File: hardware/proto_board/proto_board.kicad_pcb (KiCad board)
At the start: 2 copper layers, 120 x 70 mm, 16 parts, among them J01 Conn_02x06_Odd_Even, J010 Screw_Terminal_01x02, J02 Conn_02x06_Odd_Even, J03 Conn_02x06_Odd_Even, J04 Screw_Terminal_01x02, J05 Conn_02x06_Odd_Even, J06 Screw_Terminal_01x02, J07 Screw_Terminal_01x02, J08 Screw_Terminal_01x02, J09 Screw_Terminal_01x02

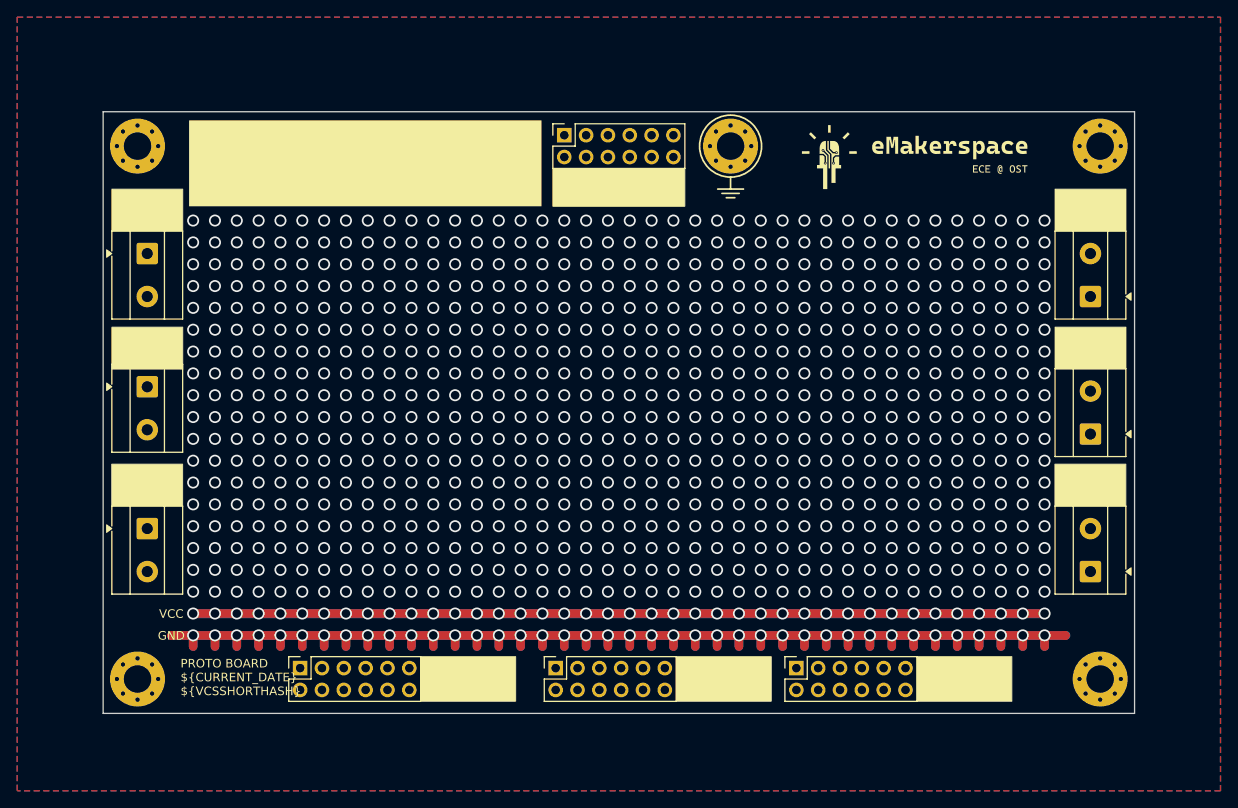
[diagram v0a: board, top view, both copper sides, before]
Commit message: Add solder pads to ribbon cable
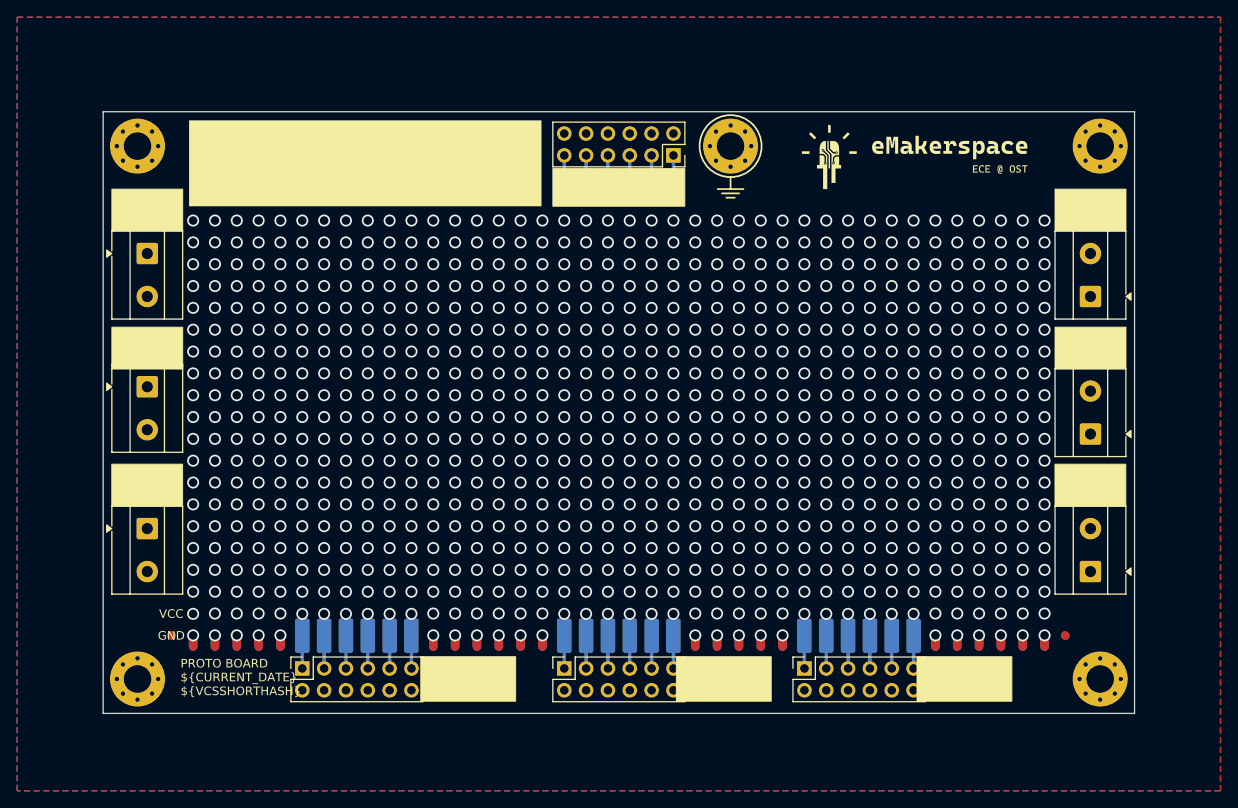
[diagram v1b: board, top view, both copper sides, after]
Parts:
- added J011: Conn_01x06, barbot:6Pin, B.Cu at (136.3, 69.9)
- added J012: Conn_01x06, barbot:6Pin, B.Cu at (93.2, 122.0)
- added J013: Conn_01x06, barbot:6Pin, B.Cu at (123.7, 122.0)
- added J014: Conn_01x06, barbot:6Pin, B.Cu at (151.6, 122.0)
- moved J05 12.9 mm to (136.3, 66.1), turned to -90 degrees
- moved J02 1.00 mm to (123.7, 125.8)
- moved J03 0.94 mm to (151.6, 125.8)
- moved J01 0.25 mm to (93.2, 125.8)
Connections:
- J01 pad 1: unconnected-(J01-Pin_1-Pad1) -> Net-(J01-Pin_1)
- J01 pad 11: unconnected-(J01-Pin_11-Pad11) -> Net-(J01-Pin_11)
- J01 pad 3: unconnected-(J01-Pin_3-Pad3) -> Net-(J01-Pin_3)
- J01 pad 5: unconnected-(J01-Pin_5-Pad5) -> Net-(J01-Pin_5)
- J01 pad 7: unconnected-(J01-Pin_7-Pad7) -> Net-(J01-Pin_7)
- J01 pad 9: unconnected-(J01-Pin_9-Pad9) -> Net-(J01-Pin_9)
- J02 pad 1: unconnected-(J02-Pin_1-Pad1) -> Net-(J013-Pin_1)
- J02 pad 11: unconnected-(J02-Pin_11-Pad11) -> Net-(J013-Pin_6)
- J02 pad 3: unconnected-(J02-Pin_3-Pad3) -> Net-(J013-Pin_2)
- J02 pad 5: unconnected-(J02-Pin_5-Pad5) -> Net-(J013-Pin_3)
- J02 pad 7: unconnected-(J02-Pin_7-Pad7) -> Net-(J013-Pin_4)
- J02 pad 9: unconnected-(J02-Pin_9-Pad9) -> Net-(J013-Pin_5)
- J03 pad 1: unconnected-(J03-Pin_1-Pad1) -> Net-(J014-Pin_1)
- J03 pad 11: unconnected-(J03-Pin_11-Pad11) -> Net-(J014-Pin_6)
- J03 pad 3: unconnected-(J03-Pin_3-Pad3) -> Net-(J014-Pin_2)
- J03 pad 5: unconnected-(J03-Pin_5-Pad5) -> Net-(J014-Pin_3)
- J03 pad 7: unconnected-(J03-Pin_7-Pad7) -> Net-(J014-Pin_4)
- J03 pad 9: unconnected-(J03-Pin_9-Pad9) -> Net-(J014-Pin_5)
- J05 pad 1: unconnected-(J05-Pin_1-Pad1) -> Net-(J011-Pin_1)
- J05 pad 11: unconnected-(J05-Pin_11-Pad11) -> Net-(J011-Pin_6)
- J05 pad 3: unconnected-(J05-Pin_3-Pad3) -> Net-(J011-Pin_2)
- J05 pad 5: unconnected-(J05-Pin_5-Pad5) -> Net-(J011-Pin_3)
- J05 pad 7: unconnected-(J05-Pin_7-Pad7) -> Net-(J011-Pin_4)
- J05 pad 9: unconnected-(J05-Pin_9-Pad9) -> Net-(J011-Pin_5)
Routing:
- net GND: track 312.9 -> 57.8 mm, vias 40 -> 22
- net (no net): track 198.1 -> 0.00 mm
- net Net-(J014-Pin_6): track 0.00 -> 3.81 mm
- net Net-(J014-Pin_5): track 0.00 -> 3.81 mm
- net Net-(J014-Pin_4): track 0.00 -> 3.81 mm
- net Net-(J014-Pin_3): track 0.00 -> 3.81 mm
- net Net-(J014-Pin_2): track 0.00 -> 3.81 mm
- net Net-(J014-Pin_1): track 0.00 -> 3.81 mm
- net Net-(J013-Pin_6): track 0.00 -> 3.81 mm
- net Net-(J013-Pin_5): track 0.00 -> 3.81 mm
- net Net-(J013-Pin_4): track 0.00 -> 3.81 mm
- net Net-(J013-Pin_3): track 0.00 -> 3.81 mm
- net Net-(J013-Pin_2): track 0.00 -> 3.81 mm
- net Net-(J013-Pin_1): track 0.00 -> 3.81 mm
- net Net-(J011-Pin_6): track 0.00 -> 3.81 mm
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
